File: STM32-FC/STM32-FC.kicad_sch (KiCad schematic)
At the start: 29 parts, among them J1 GH 1.25mm 6P, Q1 S9013, U1 STM32F407VETx, Y1 16MHz

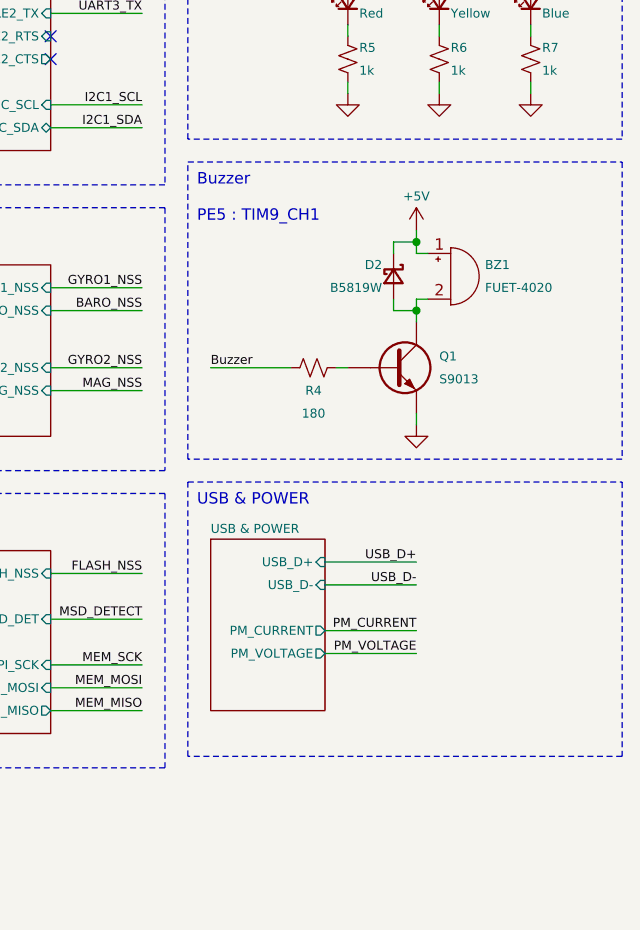
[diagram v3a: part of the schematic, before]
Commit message: update : BJT to MOSFET
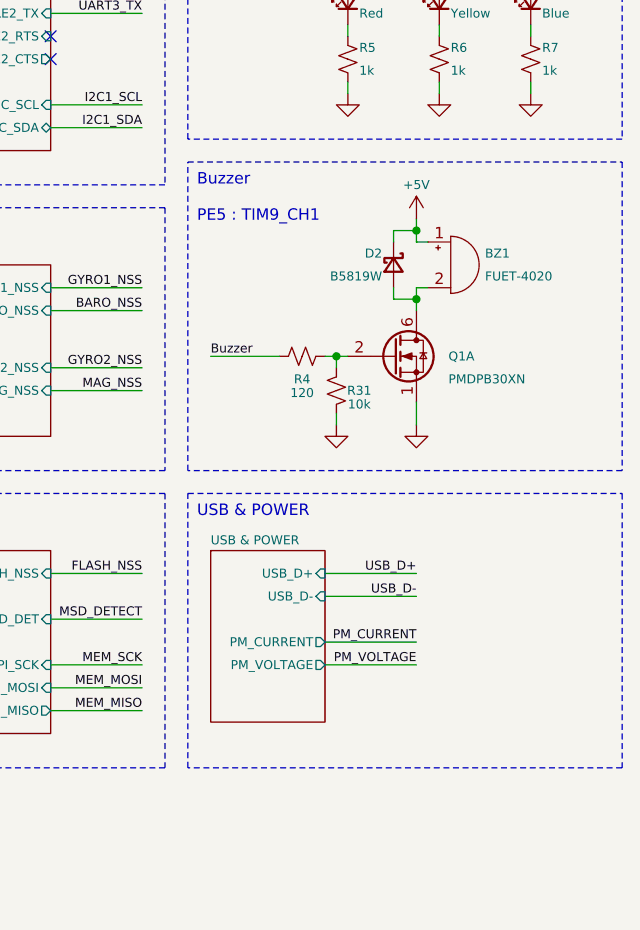
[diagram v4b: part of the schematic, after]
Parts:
- removed Q1: S9013, Package_TO_SOT_SMD:SOT-23-3, symbol Device:Q_NPN
- added Q1: PMDPB30XN, Nexperia_PMD:Nexperia_SOT1118, symbol Nexperia_PMD:PMDPB30XN
- added R31: 10k, Resistor_SMD:R_0402_1005Metric, symbol Device:R_Small_US
- R4: value 180 -> 120; LCSC C38941 -> C25079
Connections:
- net GND: now also Q1.1 (S), R31.2
- net at R4.2: now also Q1.2 (G), R31.1
- net at BZ1.2 (+), D2.2 (A): now also Q1.6 (D), Q1.7 (D)
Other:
- moved on the sheet: BZ1, D2

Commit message: WIP : pcb part layout &* BOM udpate
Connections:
- net MEM_MISO: now also U1.90 (PB4); no longer U1.53 (PB14)
- net MEM_MOSI: now also U1.91 (PB5); no longer U1.54 (PB15)
- net MEM_SCK: now also U1.89 (PB3); no longer U1.52 (PB13)
- net SEN2_MISO: now also U1.53 (PB14); no longer U1.90 (PB4)
- net SEN2_MOSI: now also U1.54 (PB15); no longer U1.91 (PB5)
- net SEN2_SCK: now also U1.52 (PB13); no longer U1.89 (PB3)

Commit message: PCB layout done
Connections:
- net BARO_NSS: now also U1.36 (PB1); no longer U1.41 (PE10)
- net FLASH_NSS: now also U1.98 (PE1); no longer U1.42 (PE11)
- net GPS1_SCL: now also U1.95 (PB8); no longer U1.47 (PB10)
- net GPS1_SDA: now also U1.96 (PB9); no longer U1.48 (PB11)
- net GYRO1_NSS: now also U1.35 (PB0); no longer U1.38 (PE7)
- net GYRO2_NSS: now also U1.43 (PE12); no longer U1.39 (PE8)
- net I2C1_SCL: now also U1.47 (PB10); no longer U1.95 (PB8)
- net I2C1_SDA: now also U1.48 (PB11); no longer U1.96 (PB9)
- net LED_BLUE: now also U1.2 (PE3); no longer U1.1 (PE2)
- net LED_YELLOW: now also U1.1 (PE2); no longer U1.98 (PE1)
- net MAG_NSS: now also U1.42 (PE11); no longer U1.40 (PE9)
- net PM_CURRENT: now also U1.18 (PC3); no longer U1.17 (PC2)
- net PM_VOLTAGE: now also U1.17 (PC2); no longer U1.18 (PC3)
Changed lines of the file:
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@@
 	)
 	(no_connect
-		(at 110.49 100.33)
-	)
-	(no_connect
-		(at 110.49 97.79)
+		(at 59.69 95.25)
 	)
 	(no_connect
@@
 	)
 	(no_connect
-		(at 59.69 85.09)
-	)
-	(no_connect
 		(at 110.49 74.93)
 	)
@@
 	)
 	(no_connect
-		(at 59.69 107.95)
+		(at 59.69 100.33)
 	)
 	(no_connect
@@
 	)
 	(no_connect
+		(at 59.69 102.87)
+	)
+	(no_connect
 		(at 110.49 115.57)
 	)
 	(no_connect
+		(at 59.69 97.79)
+	)
+	(no_connect
 		(at 110.49 140.97)
 	)
@@
 	(wire
 		(pts
+			(xy 59.69 80.01) (xy 49.53 80.01)
+		)
+		(stroke
+			(width 0)
+			(type default)
+		)
+	)
+	(wire
+		(pts
 			(xy 182.88 29.21) (xy 193.04 29.21)
 		)
@@
 	(wire
 		(pts
-			(xy 59.69 97.79) (xy 49.53 97.79)
+			(xy 59.69 107.95) (xy 49.53 107.95)
 		)
 		(stroke
@@
 	(wire
 		(pts
-			(xy 59.69 95.25) (xy 49.53 95.25)
+			(xy 110.49 97.79) (xy 120.65 97.79)
 		)
 		(stroke
@@
 	(wire
 		(pts
-			(xy 59.69 102.87) (xy 49.53 102.87)
+			(xy 110.49 100.33) (xy 120.65 100.33)
 		)
 		(stroke
@@
 	(wire
 		(pts
-			(xy 59.69 100.33) (xy 49.53 100.33)
+			(xy 59.69 105.41) (xy 49.53 105.41)
 		)
 		(stroke
@@
 	(wire
 		(pts
-			(xy 59.69 80.01) (xy 49.53 80.01)
+			(xy 59.69 82.55) (xy 49.53 82.55)
 		)
 		(stroke
@@
 	(wire
 		(pts
-			(xy 110.49 125.73) (xy 120.65 125.73)
+			(xy 110.49 120.65) (xy 120.65 120.65)
 		)
 		(stroke
@@
 	(wire
 		(pts
-			(xy 59.69 105.41) (xy 49.53 105.41)
-		)
-		(stroke
-			(width 0)
-			(type default)
-		)
-	)
-	(wire
-		(pts
-			(xy 59.69 82.55) (xy 49.53 82.55)
+			(xy 59.69 85.09) (xy 49.53 85.09)
 		)
 		(stroke
@@
 	(wire
 		(pts
-			(xy 110.49 123.19) (xy 120.65 123.19)
+			(xy 110.49 118.11) (xy 120.65 118.11)
 		)
 		(stroke
@@
 	(wire
 		(pts
-			(xy 110.49 148.59) (xy 120.65 148.59)
+			(xy 110.49 146.05) (xy 120.65 146.05)
 		)
 		(stroke
@@
 	(wire
 		(pts
-			(xy 110.49 120.65) (xy 120.65 120.65)
+			(xy 110.49 125.73) (xy 120.65 125.73)
 		)
 		(stroke
@@
 	(wire
 		(pts
-			(xy 110.49 118.11) (xy 120.65 118.11)
+			(xy 110.49 123.19) (xy 120.65 123.19)
 		)
 		(stroke
@@
 	(wire
 		(pts
-			(xy 110.49 146.05) (xy 120.65 146.05)
+			(xy 110.49 148.59) (xy 120.65 148.59)
 		)
 		(stroke
@@
 	)
 	(label "PM_VOLTAGE"
-		(at 120.65 148.59 180)
+		(at 120.65 146.05 180)
 		(effects
 			(font
@@
 	)
 	(label "I2C1_SDA"
-		(at 120.65 120.65 180)
+		(at 120.65 125.73 180)
 		(effects
 			(font
@@
 	)
 	(label "GPS1_SCL"
-		(at 120.65 123.19 180)
+		(at 120.65 118.11 180)
 		(effects
 			(font
@@
 	)
 	(label "GYRO1_NSS"
-		(at 49.53 95.25 0)
+		(at 120.65 97.79 180)
 		(effects
 			(font
 				(size 1 1)
 			)
-			(justify left bottom)
+			(justify right bottom)
 		)
 	)
@@
 	)
 	(label "GPS1_SDA"
-		(at 120.65 125.73 180)
+		(at 120.65 120.65 180)
 		(effects
 			(font
@@
 	)
 	(label "MAG_NSS"
-		(at 49.53 100.33 0)
+		(at 49.53 105.41 0)
 		(effects
 			(font
@@
 	)
 	(label "BARO_NSS"
-		(at 49.53 102.87 0)
+		(at 120.65 100.33 180)
 		(effects
 			(font
 				(size 1 1)
 			)
-			(justify left bottom)
+			(justify right bottom)
 		)
 	)
@@
 	)
 	(label "PM_CURRENT"
-		(at 120.65 146.05 180)
+		(at 120.65 148.59 180)
 		(effects
 			(font
@@
 	)
 	(label "GYRO2_NSS"
-		(at 49.53 97.79 0)
+		(at 49.53 107.95 0)
+		(effects
+			(font
+				(size 1 1)
+			)
+			(justify left bottom)
+		)
+	)
+	(label "FLASH_NSS"
+		(at 49.53 80.01 0)
 		(effects
 			(font
@@
 	)
 	(label "I2C1_SCL"
-		(at 120.65 118.11 180)
+		(at 120.65 123.19 180)
 		(effects
 			(font
@@
 	)
 	(label "LED_BLUE"
-		(at 49.53 82.55 0)
+		(at 49.53 85.09 0)
 		(effects
 			(font
@@
 	)
 	(label "LED_YELLOW"
-		(at 49.53 80.01 0)
+		(at 49.53 82.55 0)
 		(effects
 			(font
@@
 		)
 	)
-	(label "FLASH_NSS"
-		(at 49.53 105.41 0)
-		(effects
-			(font
-				(size 1 1)
-			)
-			(justify left bottom)
-		)
-	)

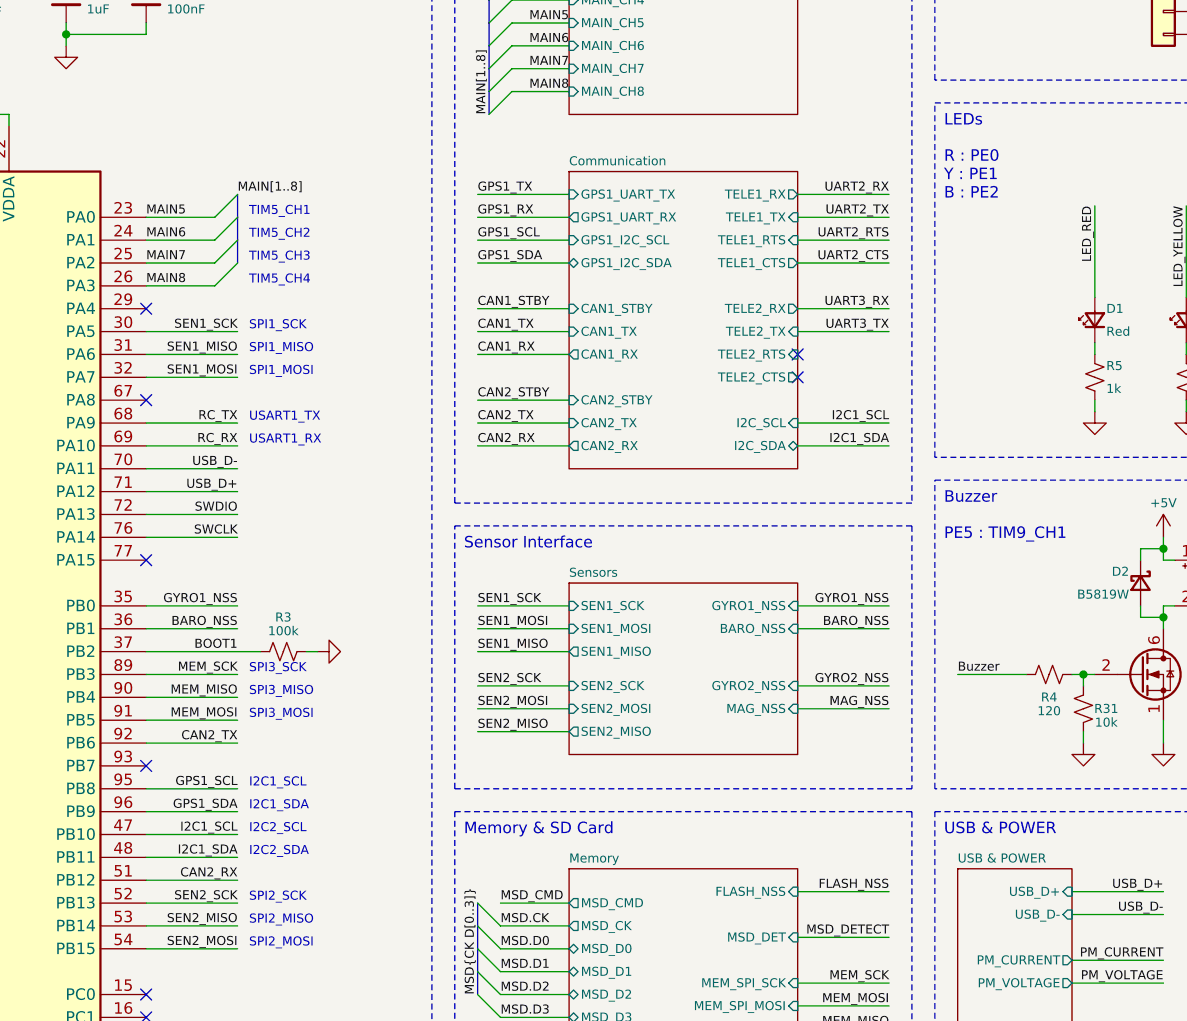
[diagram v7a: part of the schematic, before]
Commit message: fix : readme & schematic minor fix
- schematic comment fix
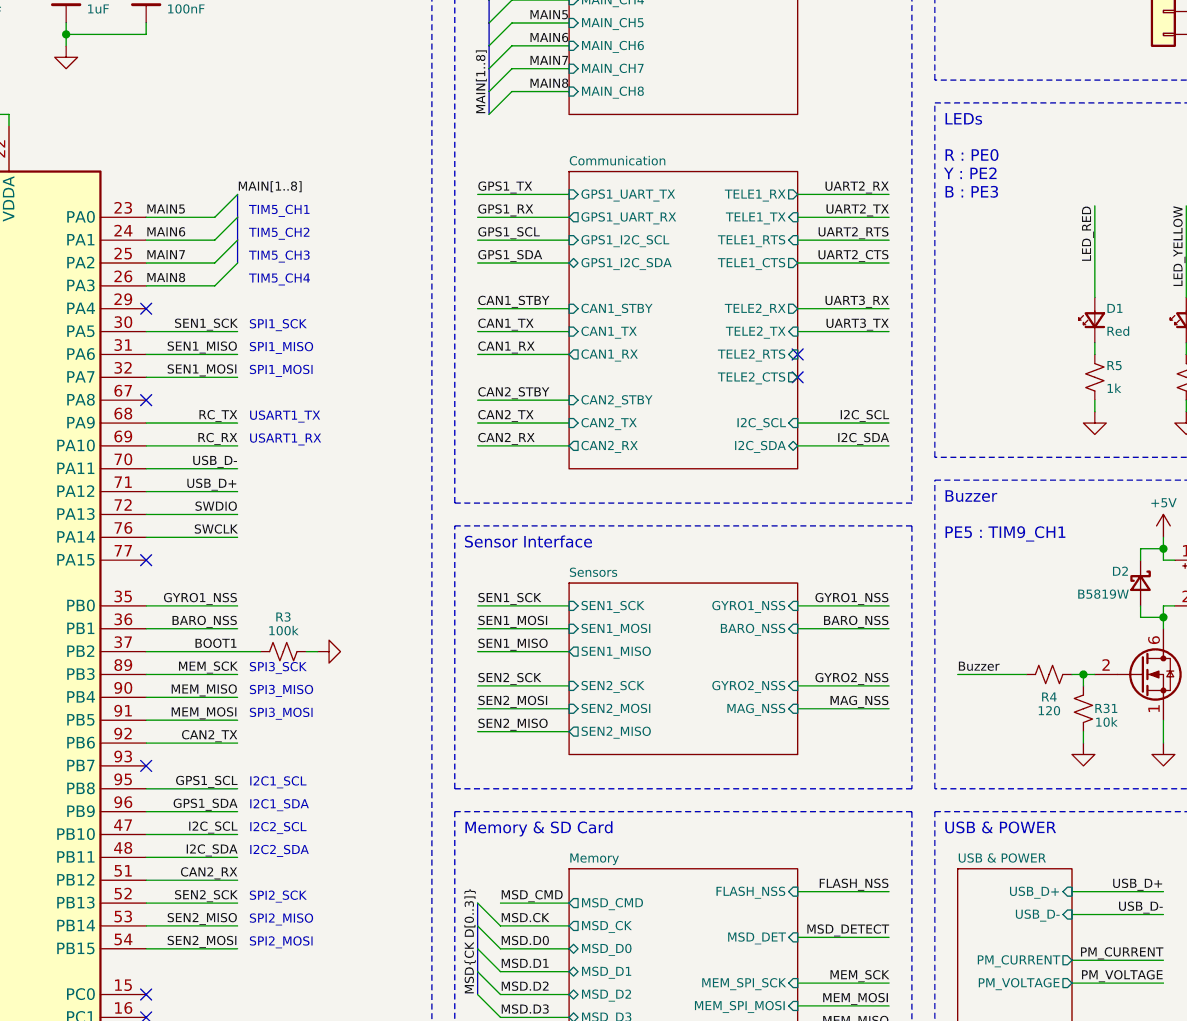
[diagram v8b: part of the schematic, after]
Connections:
- net I2C1_SCL renamed I2C_SCL
- net I2C1_SDA renamed I2C_SDA
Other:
- note added: "R : PE0 Y : PE2 B : PE3"
- note removed: "R : PE0 Y : PE1 B : PE2"
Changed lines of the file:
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@@
 	(title_block
 		(title "NARAEON - Flight Controller")
-		(date "2025-10-10")
+		(date "2025-10-11")
 		(rev "v1.1.0")
 		(company "NARAE UAV Project ")
 		(comment 1 "INHA Univ. Areo-modelling Club")
-		(comment 2 "* Work in progress")
+		(comment 2 "github.com/NARAE-INHA-UNIV")
 	)
 	(rectangle
@@
 		)
 	)
-	(text "R : PE0\nY : PE1\nB : PE2"
+	(text "R : PE0\nY : PE2\nB : PE3"
 		(exclude_from_sim no)
 		(at 199.136 47.244 0)
@@
 		)
 	)
-	(label "I2C1_SCL"
+	(label "I2C_SCL"
 		(at 193.04 77.47 180)
 		(effects
@@
 		)
 	)
-	(label "I2C1_SDA"
+	(label "I2C_SDA"
 		(at 120.65 125.73 180)
 		(effects
@@
 		)
 	)
-	(label "I2C1_SCL"
+	(label "I2C_SCL"
 		(at 120.65 123.19 180)
 		(effects
@@
 		)
 	)
-	(label "I2C1_SDA"
+	(label "I2C_SDA"
 		(at 193.04 80.01 180)
 		(effects
